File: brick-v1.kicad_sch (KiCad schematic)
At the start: 15 parts, among them J1 buzzer_toggle_pin, J2 battery_header, U1 Teensy4.1, U2 voltReg

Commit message: v1.3 update
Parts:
- removed J1: buzzer_toggle_pin, Connector_PinHeader_2.54mm:PinHeader_1x03_P2.54mm_Vertical, symbol rrc_pcb-rescue:Conn_01x03_Male-Connector
- removed R1, R2: R-Device, Resistor_THT:R_Axial_DIN0207_L6.3mm_D2.5mm_P10.16mm_Horizontal, symbol rrc_pcb-rescue:R-Device
- removed S1: RFD900+-RF_Module, rrc_rfd900+:RFD900+, symbol parts:RFD900+-RF_Module
- removed U2: voltReg, rrc_voltReg:voltReg2, symbol parts:voltReg
- added R3: R-Device, Resistor_THT:R_Axial_DIN0207_L6.3mm_D2.5mm_P10.16mm_Horizontal, symbol rrc_pcb-rescue:R-Device
- added TH1: Thermistor, Resistor_THT:R_Axial_DIN0922_L20.0mm_D9.0mm_P25.40mm_Horizontal, symbol Device:Thermistor
- added U1: XB3-24Z8CM-J, RRC_footprint:xbee_s2c, symbol Library:XB3-24Z8CM-J
- added U2: L7805, Connector_PinHeader_2.54mm:PinHeader_1x03_P2.54mm_Vertical, symbol Regulator_Linear:L7805
- Logo1: renamed from Logo0; footprint rrc_logo:RRC_logo -> rrc_logo:tmu
- renumbered I2 to I1, I1 to I2, J2 to J1, R3 to R1, R4 to R2, S2 to S1, U1 to U3
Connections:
- net SDA2 is gone; now on net SCL2: I3.4 (SDA), R2.1, U3.25 (25_A11_RX6_SDA2)
- net T_VCC is gone; now on net SCL2: I1.1 (VCC), I2.3 (VCC), I3.1 (VCC), R1.2, R2.2, U3.3.3V_1 (3V3), U3.3.3V_2 (3V3)
- net GND: now also R3.1, TH1.1, U1.1 (GND), U1.10 (GND), U1.12 (GND), U1.21 (GND), U1.32 (GND), U1.34 (GND), U2.2 (GND)
- net RX2: now also U1.31 (AD0/DIO0)
- net SCL2: now also I1.3 (SCL), I1.4 (SDA)
- net TX2: now also U1.30 (AD1/DIO1)
- net V+: now also I2.1 (VIN+), J1.2 (Pin_2), U2.1 (IN); no longer I2.2 (VIN-)
- net V-: now also I2.2 (VIN-), J1.1 (Pin_1), R3.2; no longer J1.2 (Pin_2)
- net VCC: now also U1.2 (VCC), U2.3 (OUT)
- net at U3.27 (27_A13_SCK1): now also TH1.2
- net SCL1: no longer names the net of U3.16 (16_A2_RX4_SCL1)
- net SCL1: no longer I1.3 (SCL)
- net SDA1: no longer names the net of U3.17 (17_A3_TX4_SDA1)
- net SDA1: no longer I1.4 (SDA)
- no-connect marks 69 -> 59
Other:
- note added: "MOTORS+ESC"
- company: Metrocketry -> MIMS lab
- title: Brick -> Flight controller
- moved on the sheet: J1, Logo1, S1

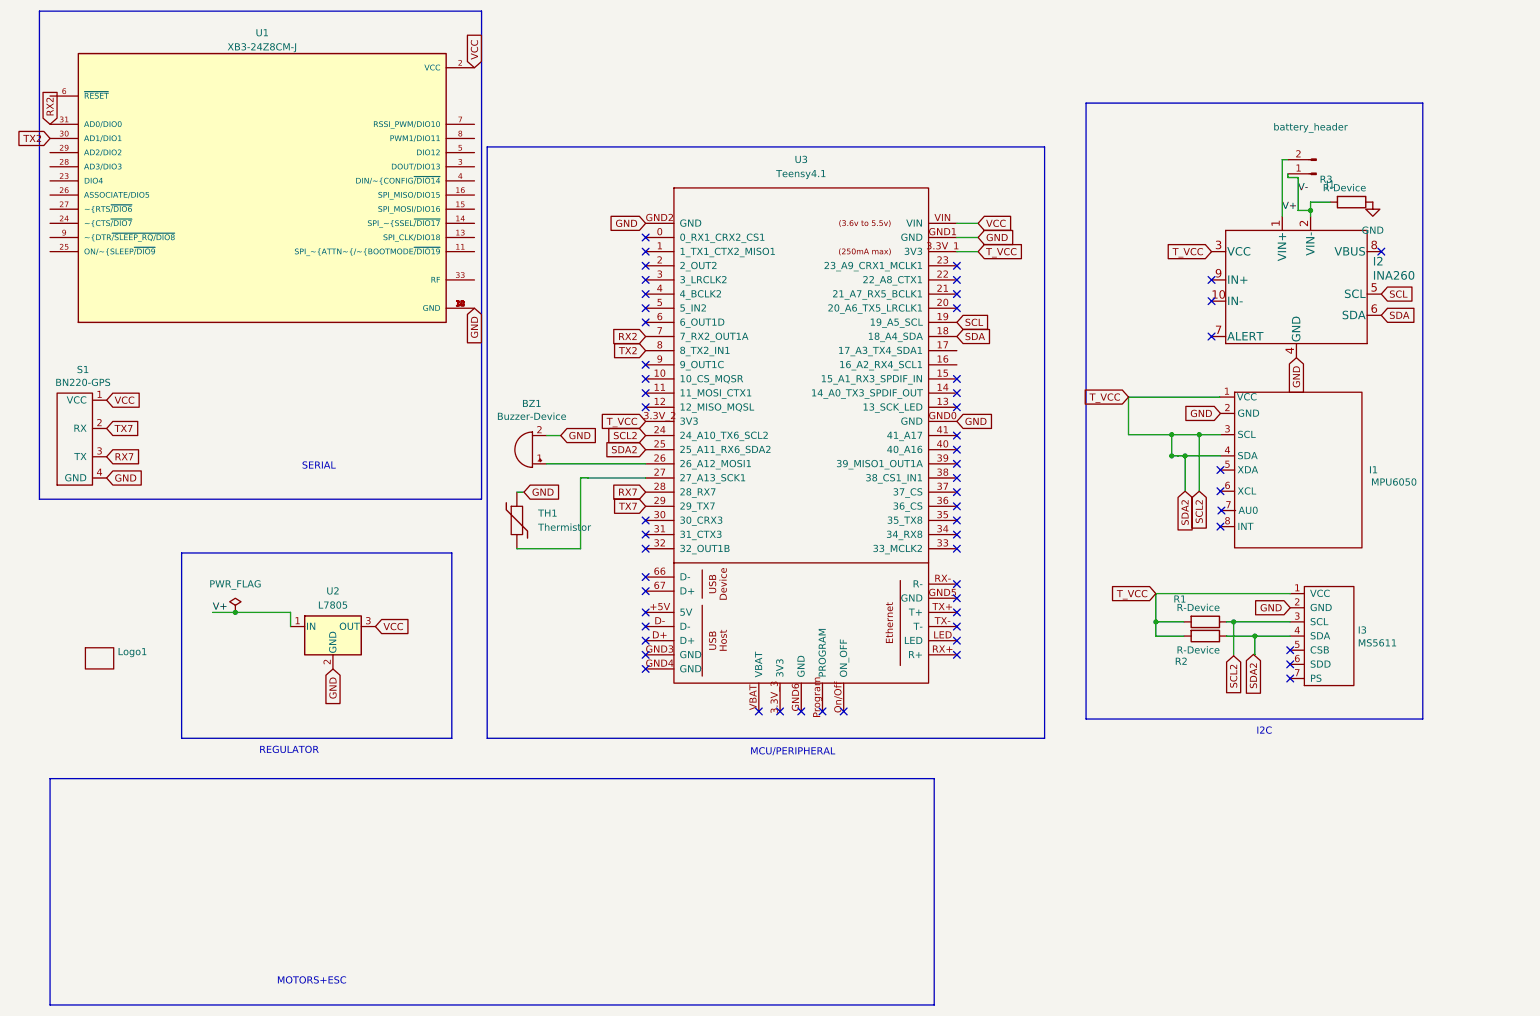
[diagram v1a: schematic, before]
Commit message: updated traces
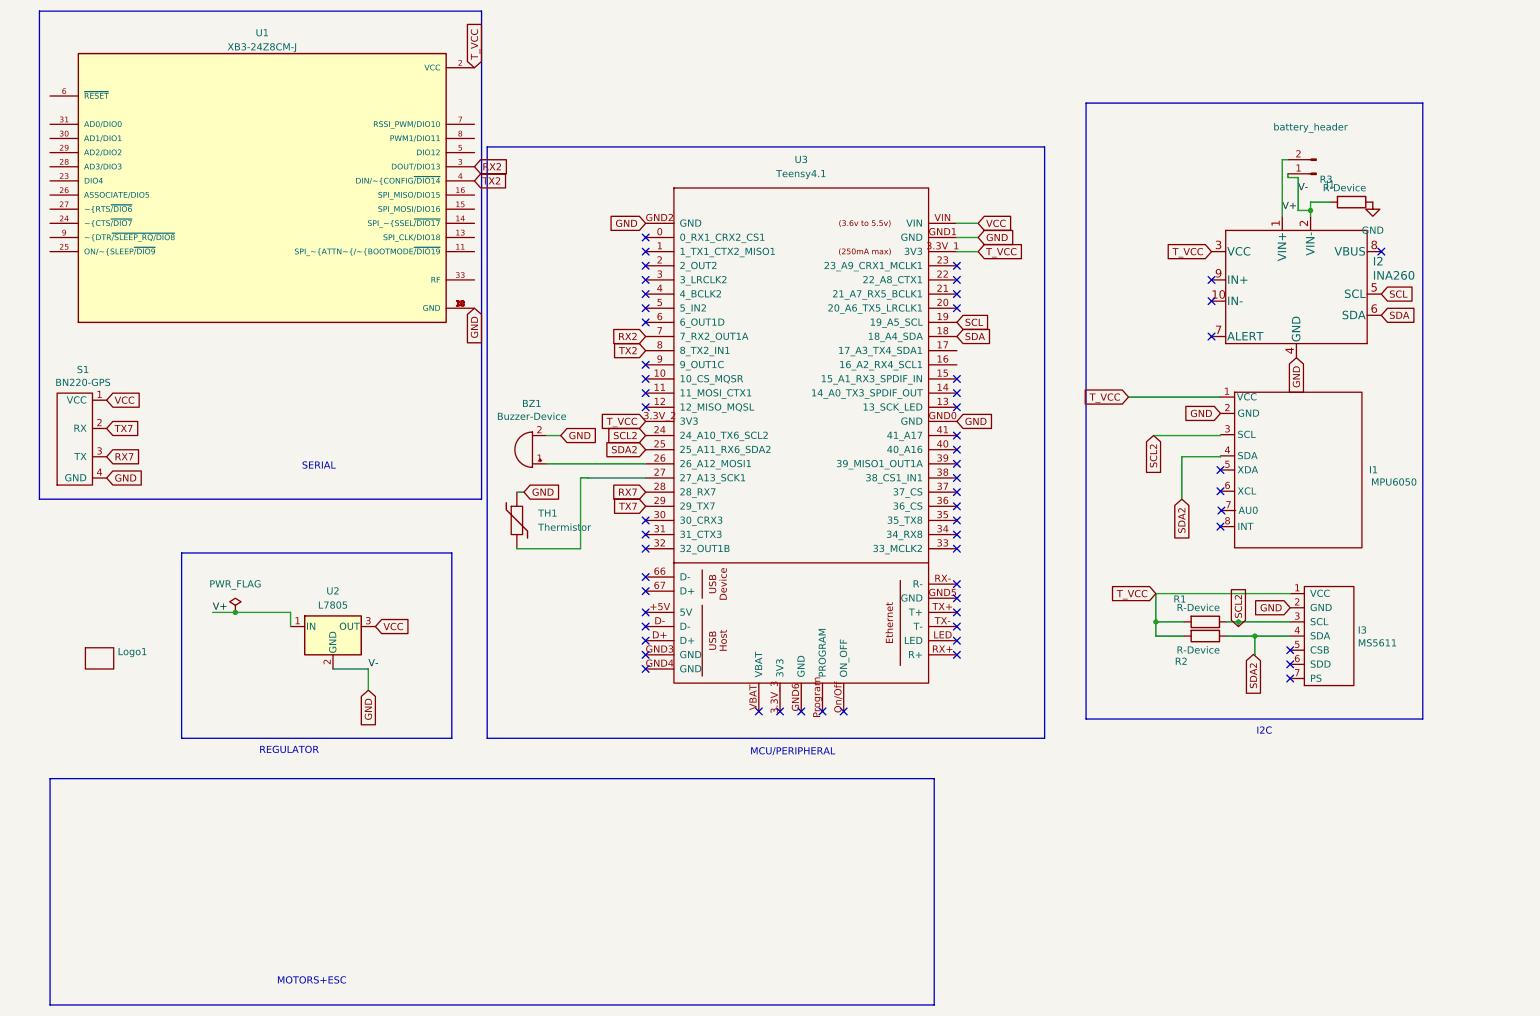
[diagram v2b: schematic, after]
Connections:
- net V- is gone; now on net GND: I2.2 (VIN-), J1.1 (Pin_1), R3.2
- net RX2: now also U1.3 (DOUT/DIO13); no longer U1.31 (AD0/DIO0)
- net SCL2: no longer I1.1 (VCC), I1.4 (SDA), I2.3 (VCC), I3.1 (VCC), I3.4 (SDA), R1.2, R2.1, R2.2, U3.25 (25_A11_RX6_SDA2), U3.3.3V_1 (3V3), U3.3.3V_2 (3V3)
- net TX2: now also U1.4 (DIN/~{CONFIG~{/DIO14}); no longer U1.30 (AD1/DIO1)
- net VCC: no longer U1.2 (VCC)
- new net SDA2: I1.4 (SDA), I3.4 (SDA), R2.1, U3.25 (25_A11_RX6_SDA2)
- new net T_VCC: I1.1 (VCC), I2.3 (VCC), I3.1 (VCC), R1.2, R2.2, U1.2 (VCC), U3.3.3V_1 (3V3), U3.3.3V_2 (3V3)

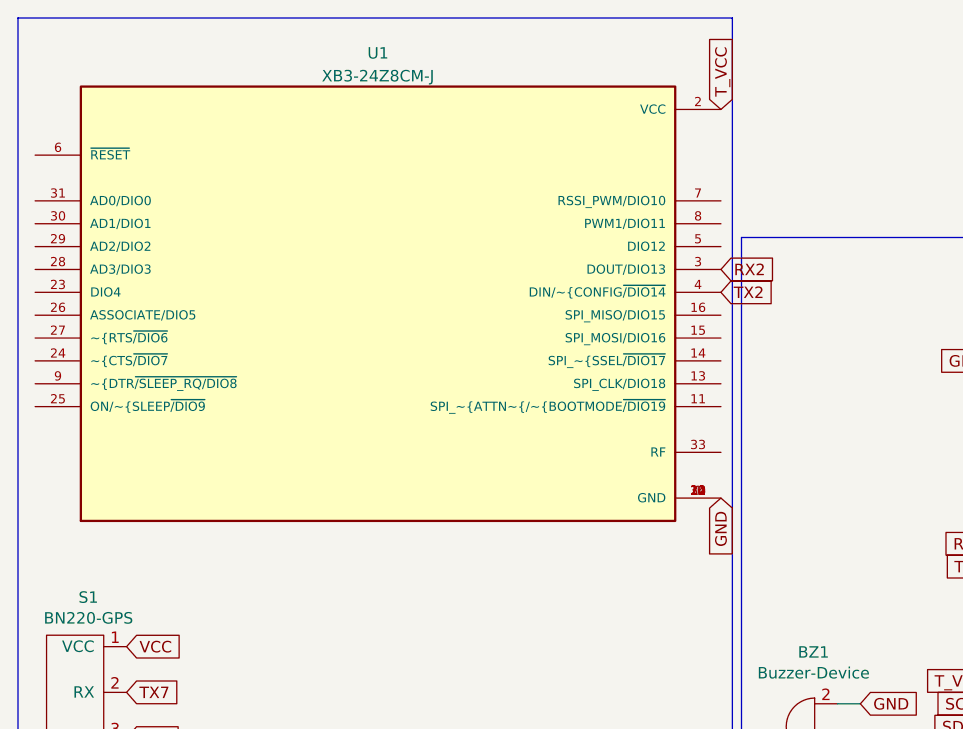
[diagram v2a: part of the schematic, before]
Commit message: editted footprints and symbol of xbee
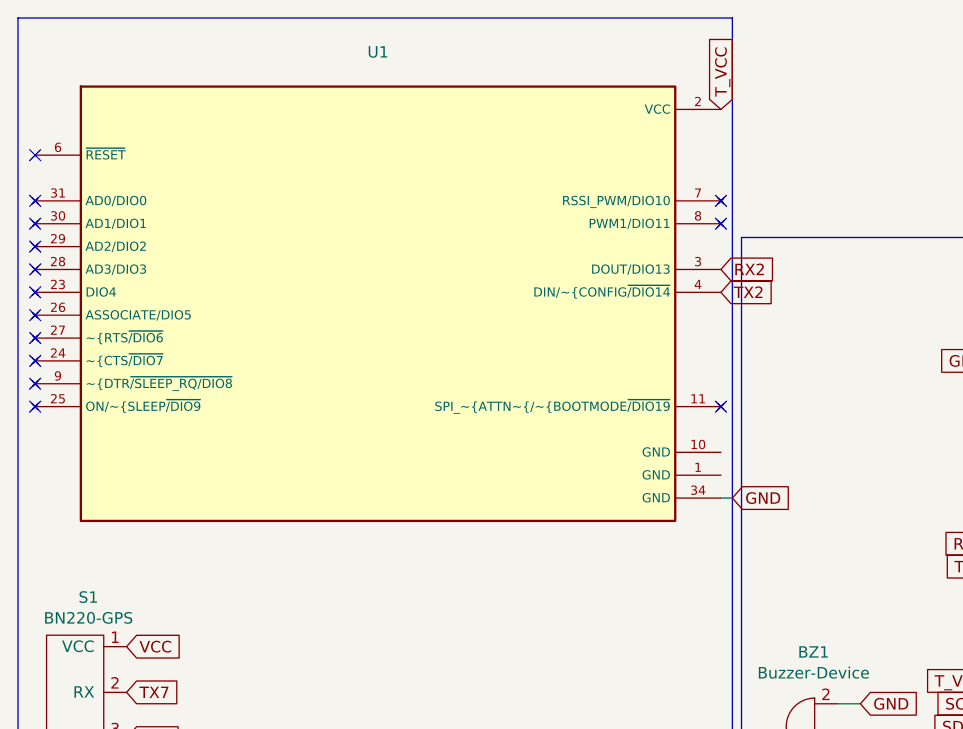
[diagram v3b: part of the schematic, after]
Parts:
- removed U1: XB3-24Z8CM-J, RRC_footprint:xbee_s2c, symbol Library:XB3-24Z8CM-J
- added U1: ~, RRC_footprint:xbee_s2c, symbol parts:xbee_s2c
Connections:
- net GND: now also U1.34 (GND)
- net RX2: now also U1.3 (DOUT/DIO13)
- net TX2: now also U1.4 (DIN/~{CONFIG~{/DIO14})
- net T_VCC: now also U1.2 (VCC)
- no-connect marks 59 -> 73
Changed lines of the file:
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@@
+	)
+	(no_connect
+		(at 16.51 39.37)
 	)
 	(no_connect
@@
 	)
 	(no_connect
+		(at 92.71 39.37)
+	)
+	(no_connect
 		(at 151.384 142.24)
 	)
 	(no_connect
+		(at 16.51 49.53)
+	)
+	(no_connect
 		(at 123.444 110.49)
 	)
@@
 	)
 	(no_connect
+		(at 16.51 57.15)
+	)
+	(no_connect
 		(at 123.444 69.85)
 	)
 	(no_connect
+		(at 16.51 54.61)
+	)
+	(no_connect
 		(at 225.044 68.58)
 	)
@@
 	)
 	(no_connect
+		(at 16.51 41.91)
+	)
+	(no_connect
 		(at 123.444 118.11)
 	)
@@
 	)
 	(no_connect
+		(at 16.51 59.69)
+	)
+	(no_connect
 		(at 123.444 132.08)
 	)
@@
 	)
 	(no_connect
+		(at 16.51 44.45)
+	)
+	(no_connect
+		(at 92.71 59.69)
+	)
+	(no_connect
 		(at 225.044 64.77)
 	)
@@
 	)
 	(no_connect
+		(at 92.71 36.83)
+	)
+	(no_connect
 		(at 123.444 127)
 	)
 	(no_connect
+		(at 16.51 31.75)
+	)
+	(no_connect
 		(at 179.324 92.71)
 	)
@@
 	)
 	(no_connect
+		(at 16.51 52.07)
+	)
+	(no_connect
 		(at 239.171 133.7878)
 	)
@@
 	)
 	(no_connect
+		(at 16.51 46.99)
+	)
+	(no_connect
 		(at 179.324 132.08)
 	)
 	(no_connect
+		(at 16.51 36.83)
+	)
+	(no_connect
 		(at 123.444 107.95)
 	)
@@
 		(pts
 			(xy 215.041 128.7078) (xy 215.041 126.1678)
+		)
+		(stroke
+			(width 0)
+			(type default)
+		)
+	)
+	(wire
+		(pts
+			(xy 92.71 69.85) (xy 93.98 69.85)
 		)
 		(stroke
@@
 	(global_label "GND"
 		(shape input)
-		(at 92.71 69.85 270)
-		(fields_autoplaced yes)
-		(effects
-			(font
-				(size 1.27 1.27)
-			)
-			(justify right)
-		)
-		(property "Intersheetrefs" "${INTERSHEET_REFS}"
-			(at 92.71 76.0515 90)
-			(effects
-				(font
-					(size 1.27 1.27)
-				)
-				(justify right)
+		(at 93.98 69.85 0)
+		(fields_autoplaced yes)
+		(effects
+			(font
+				(size 1.27 1.27)
+			)
+			(justify left)
+		)
+		(property "Intersheetrefs" "${INTERSHEET_REFS}"
+			(at 100.1815 69.85 0)
+			(effects
+				(font
+					(size 1.27 1.27)
+				)
+				(justify left)
 				(hide yes)
 			)
@@
 	)
 	(symbol
-		(lib_id "Library:XB3-24Z8CM-J")
-		(at 54.61 49.53 0)
+		(lib_id "parts:xbee_s2c")
+		(at 16.51 31.75 0)
 		(unit 1)
 		(exclude_from_sim no)
@@
 		(fields_autoplaced yes)
 		(property "Reference" "U1"
-			(at 54.61 20.4302 0)
-			(effects
-				(font
-					(size 1.27 1.27)
-				)
-			)
-		)
-		(property "Value" "XB3-24Z8CM-J"
-			(at 54.61 22.9671 0)
+			(at 54.61 20.32 0)
+			(effects
+				(font
+					(size 1.27 1.27)
+				)
+			)
+		)
+		(property "Value" "~"
+			(at 54.61 22.86 0)
 			(effects
 				(font
@@
 		)
 		(property "Footprint" "RRC_footprint:xbee_s2c"
-			(at 40.64 83.82 0)
-			(effects
-				(font
-					(size 1.27 1.27)
-				)
-				(justify bottom)
+			(at 16.51 31.75 0)
+			(effects
+				(font
+					(size 1.27 1.27)
+				)
 				(hide yes)
 			)
 		)
 		(property "Datasheet" ""
-			(at 54.61 49.53 0)
+			(at 16.51 31.75 0)
 			(effects
 				(font
@@
 		)
 		(property "Description" ""
-			(at 54.61 49.53 0)
-			(effects
-				(font
-					(size 1.27 1.27)
-				)
-			)
-		)
-		(property "STANDARD" "Manufacturer Recommendations"
-			(at 57.15 88.9 0)
-			(effects
-				(font
-					(size 1.27 1.27)
-				)
-				(justify bottom)
-				(hide yes)
-			)
-		)
-		(property "MANUFACTURER" "DIGI INTERNATIONAL"
-			(at 74.93 83.82 0)
-			(effects
-				(font
-					(size 1.27 1.27)
-				)
-				(justify bottom)
-				(hide yes)
-			)
-		)
-		(property "PARTREV" "N/A"
-			(at 50.8 81.28 0)
-			(effects
-				(font
-					(size 1.27 1.27)
-				)
-				(justify bottom)
-				(hide yes)
-			)
-		)
-		(property "MAXIMUM_PACKAGE_HEIGHT" "2.21mm"
-			(at 50.8 81.28 0)
-			(effects
-				(font
-					(size 1.27 1.27)
-				)
-				(justify bottom)
-				(hide yes)
-			)
+			(at 16.51 31.75 0)
+			(effects
+				(font
+					(size 1.27 1.27)
+				)
+				(hide yes)
+			)
+		)
+		(pin "10"
+		)
+		(pin "6"
+		)
+		(pin "4"
 		)
 		(pin "1"
 		)
-		(pin "10"
+		(pin "23"
+		)
+		(pin "26"
+		)
+		(pin "34"
+		)
+		(pin "24"
+		)
+		(pin "3"
+		)
+		(pin "2"
+		)
+		(pin "28"
+		)
+		(pin "9"
+		)
+		(pin "31"
+		)
+		(pin "27"
+		)
+		(pin "29"
+		)
+		(pin "25"
+		)
+		(pin "7"
+		)
+		(pin "8"
+		)
+		(pin "30"
 		)
 		(pin "11"
 		)
-		(pin "12"
-		)
-		(pin "13"
-		)
-		(pin "14"
-		)
-		(pin "15"
-		)
-		(pin "16"
-		)
-		(pin "2"
-		)
-		(pin "21"
-		)
-		(pin "23"
-		)
-		(pin "24"
-		)
-		(pin "25"
-		)
-		(pin "26"
-		)
-		(pin "27"
-		)
-		(pin "28"
-		)
-		(pin "29"
-		)
-		(pin "3"
-		)
-		(pin "30"
-		)
-		(pin "31"
-		)
-		(pin "32"
-		)
-		(pin "33"
-		)
-		(pin "34"
-		)
-		(pin "4"
-		)
-		(pin "5"
-		)
-		(pin "6"
-		)
-		(pin "7"
-		)
-		(pin "8"
-		)
-		(pin "9"
-		)
 		(instances
-			(project "brick-v1"
+			(project ""
 				(path "/03c52831-5dc5-43c5-a442-8d23643b46fb"
 					(reference "U1")
